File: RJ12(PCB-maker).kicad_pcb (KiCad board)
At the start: 2 copper layers, 21.6 x 27.9 mm, 2 parts, among them J1 Conn_02x06_Top_Bottom, P1 RJ12_Housing

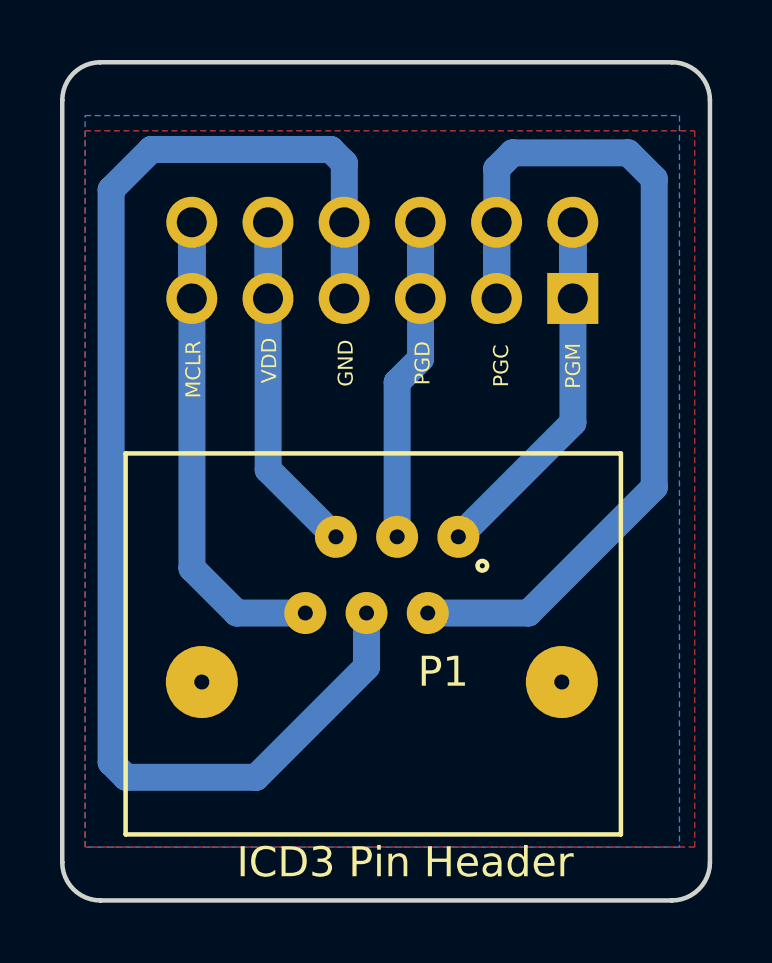
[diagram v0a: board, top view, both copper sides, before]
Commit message: Re-design the rj12 housing
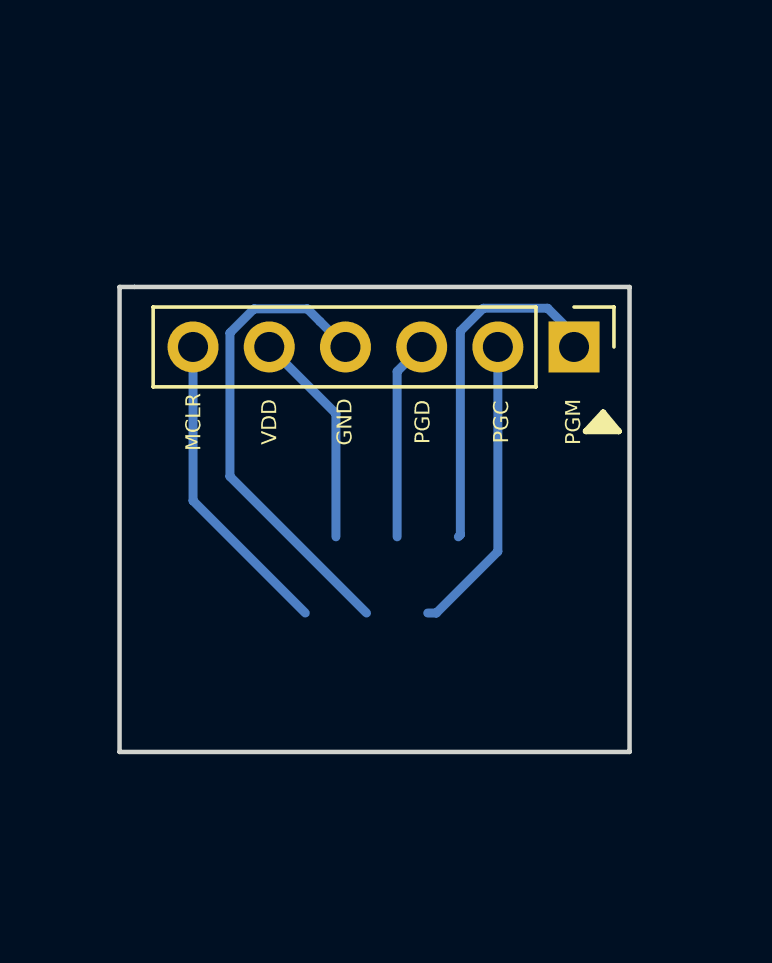
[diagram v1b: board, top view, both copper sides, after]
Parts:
- removed P1: RJ12_Housing, rj12connector:myRJ12
- J1: value Conn_02x06_Top_Bottom -> Conn_01x06; footprint Pin_Headers:Pin_Header_Straight_2x06_Pitch2.54mm -> Pin_Headers:Pin_Header_Straight_1x06_Pitch2.54mm; moved to F.Cu
- moved J1 1.62 mm to (38.6, 26.0), turned to 270 degrees
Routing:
- net pin4: track 47.0 -> 15.9 mm
- net pin2: track 32.6 -> 10.0 mm
- net pin6: track 18.2 -> 10.4 mm
- net pin5: track 13.7 -> 7.25 mm
- net pin3: track 13.0 -> 6.67 mm
- net pin1: track 14.3 -> 11.8 mm
- removed copper zone on B.Cu, net (none)
- removed copper zone on F.Cu, net (none)
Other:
- board size 21.6 x 27.9 mm -> 17 x 15.5 mm
- board text added: "ICD3 Conn"
- board text removed: "ICD3 Pin Header"
